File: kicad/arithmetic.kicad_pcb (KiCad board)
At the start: 2 copper layers, 49.5 x 53 mm, 71 parts, among them J1 Conn_01x03_Male, J2 Conn_01x05_Male, J3 Conn_01x05_Male, J4 Conn_Coaxial, J5 Conn_Coaxial, J6 Conn_Coaxial, U1 LM317, U2 LM337, U3 OPA197xD, U4 OPA197xD, U5 OPA197xD

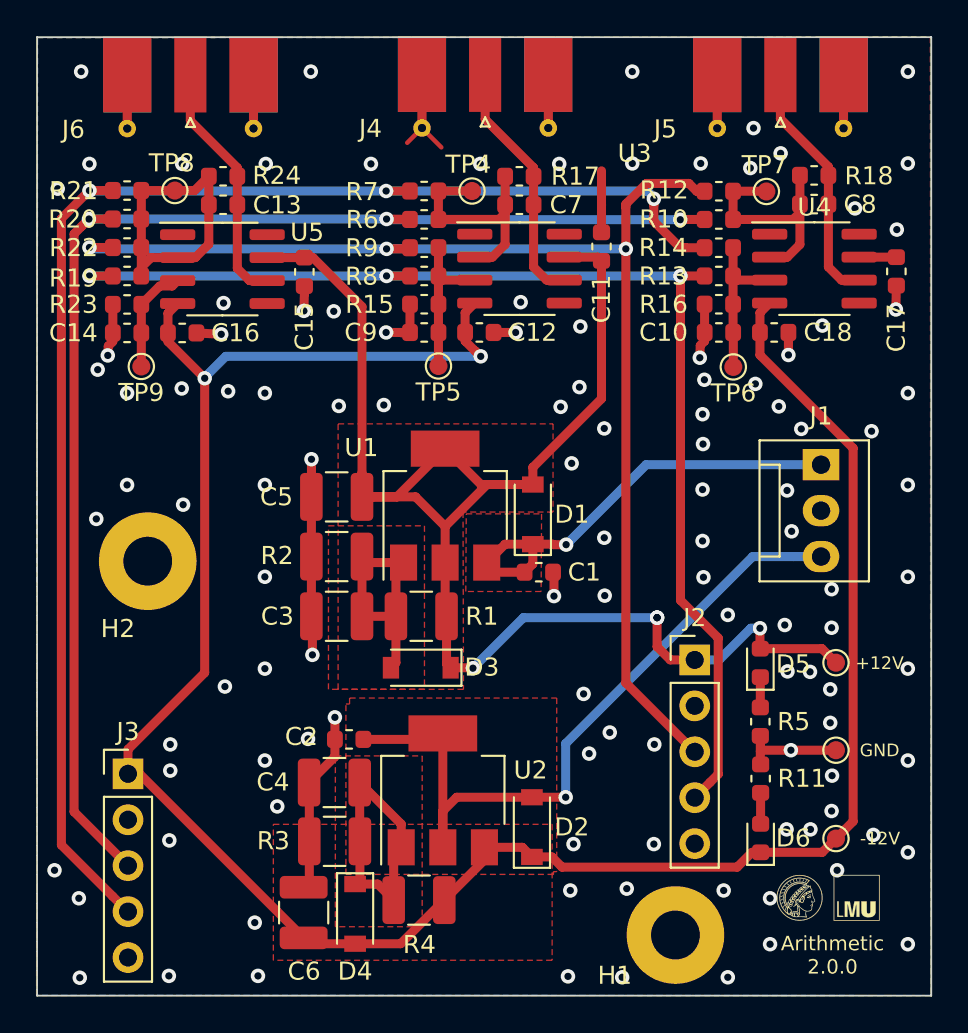
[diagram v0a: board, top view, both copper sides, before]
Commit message: moved detector mount on arithmetic to the right
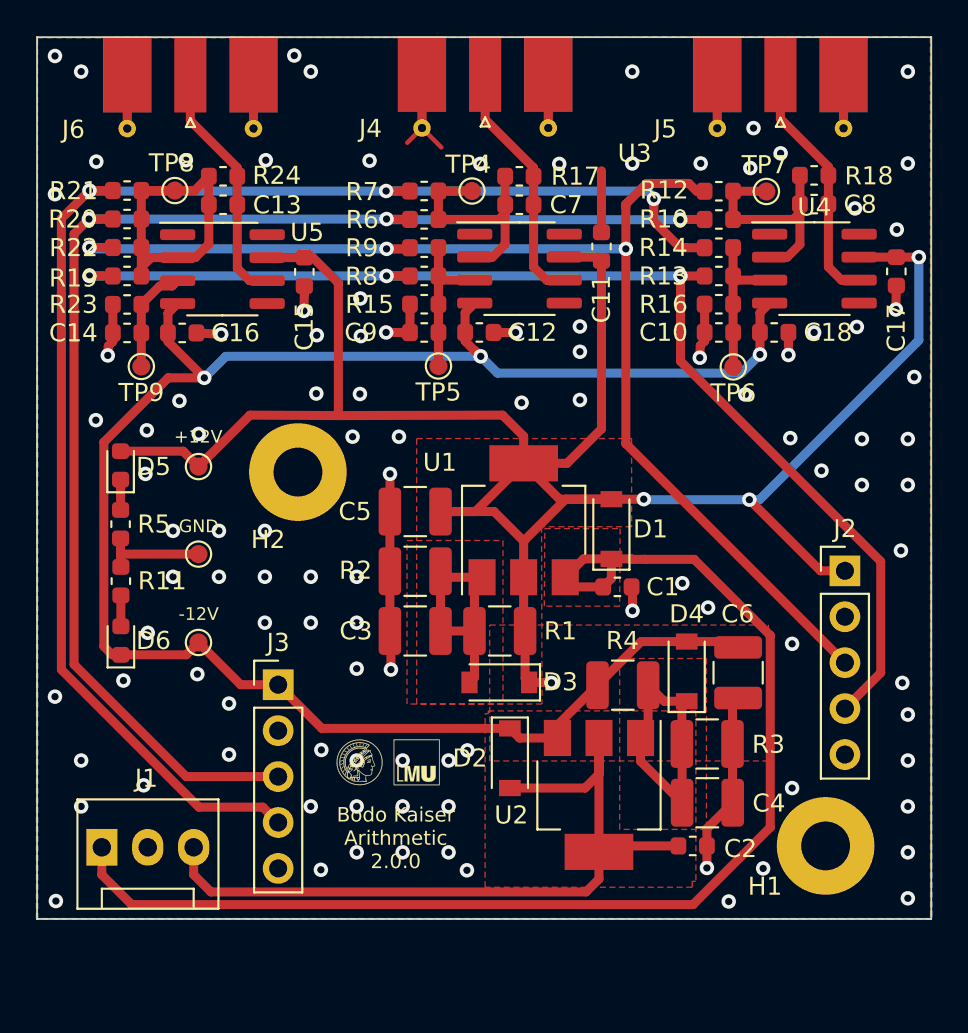
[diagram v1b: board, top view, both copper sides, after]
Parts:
- moved J1 45.1 mm to (77.3, 124.2), turned to 0 degrees
- moved R11 37.0 mm to (78.4, 109.5)
- moved D5 37.0 mm to (78.4, 103.1)
- moved D6 37.0 mm to (78.4, 112.7)
- moved R5 37.0 mm to (78.4, 106.3)
- moved +12V 36.9 mm to (82.7, 103.1)
- moved -12V 36.9 mm to (82.7, 112.9)
- moved GND 36.9 mm to (82.7, 108.0)
- moved C6 27.4 mm to (112.5, 114.5), turned to 90 degrees
- moved G*** 25.5 mm to (93.2, 119.5)
- moved D4 22.7 mm to (109.7, 114.5), turned to 90 degrees
- moved R3 21.3 mm to (110.8, 118.5), turned to 180 degrees
- moved C4 20.7 mm to (110.8, 121.7), turned to 180 degrees
- moved C2 19.9 mm to (110.0, 124.1), turned to 180 degrees
- moved R4 16.4 mm to (106.2, 115.2), turned to 180 degrees
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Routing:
- net +15V: track 24.8 -> 69.1 mm, vias 1 -> 0
- net +12V: track 92.0 -> 121.4 mm
- net -12V: track 127.4 -> 102.8 mm, vias 2 -> 3
- net -15V: track 41.3 -> 44.2 mm, vias 1 -> 0
- net /-X2: track 74.1 -> 75.6 mm
- net /-Y2: track 69.2 -> 67.7 mm
- net /-X1: track 66.9 -> 66.0 mm
- net /-Y1: track 80.9 -> 81.5 mm
- net GND: track 68.3 -> 68.4 mm, vias 116 -> 108
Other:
- board size 49.5 x 53 mm -> 49.5 x 48.8 mm
- board text added: "Bodo Kaiser Arithmetic 2.0.0"
- board text removed: "Arithmetic 2.0.0"

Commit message: fix some DRC errors, remove some test points
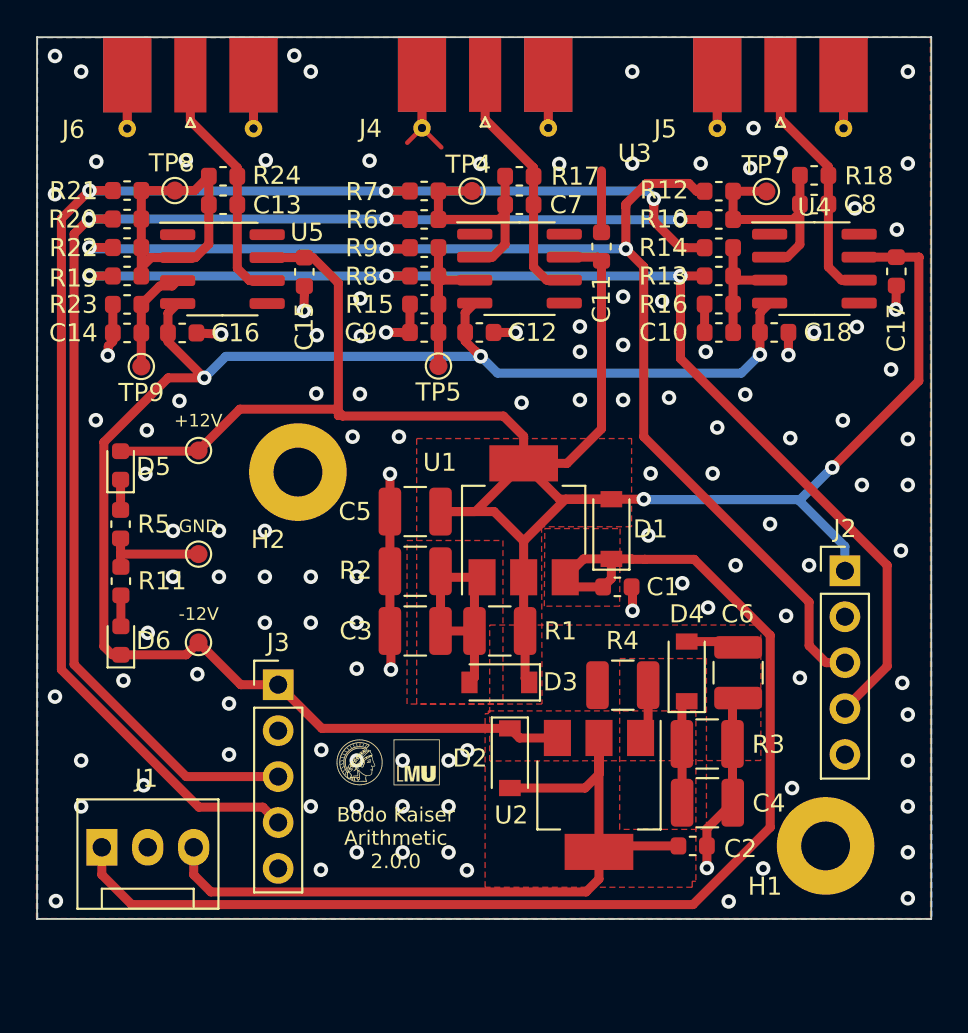
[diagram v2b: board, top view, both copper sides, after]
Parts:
- removed TP6: DIFFY+, TestPoint:TestPoint_Pad_D1.0mm
- moved +12V 0.89 mm to (82.7, 102.2)
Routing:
- net -12V: track 102.8 -> 93.0 mm
- net Net-(C4-Pad2): track 15.9 -> 8.82 mm
- net +12V: track 121.4 -> 119.2 mm, vias 4 -> 2
- net Net-(C10-Pad2): track 8.71 -> 6.80 mm
- net GND: track 68.4 -> 66.9 mm, vias 108 -> 119
- net /-Y2: track 67.7 -> 68.4 mm

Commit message: applied suggestions from Bodo Hecker
* changed R23 to 2k
* replaced pin holes in detector with padded pin holes
* increased casing of led resistors to 1210
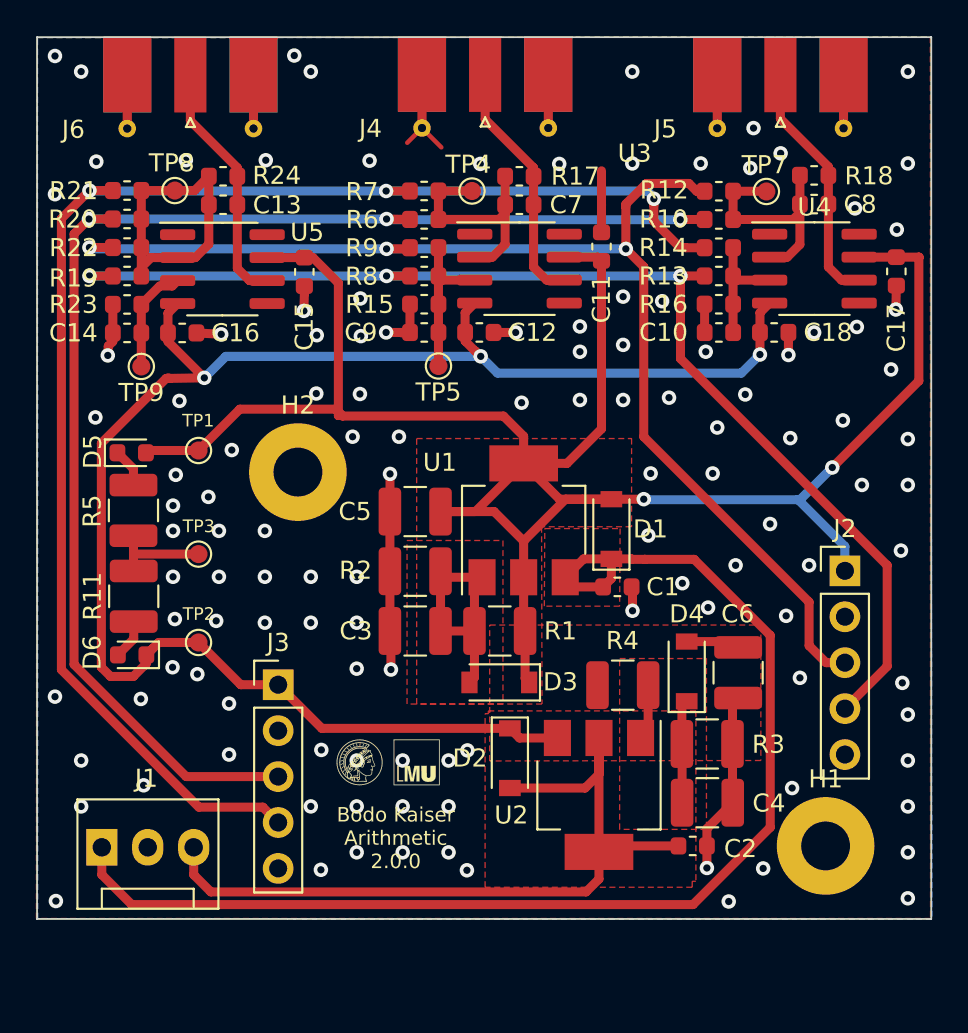
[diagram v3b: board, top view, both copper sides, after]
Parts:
- R11, R5: footprint Resistor_SMD:R_0603_1608Metric -> Resistor_SMD:R_1210_3225Metric
- R23: value 10k -> 2k
- moved R11 1.10 mm to (79.1, 110.3)
- moved R5 1.04 mm to (79.1, 105.5)
- moved D6 1.01 mm to (79.0, 113.5), turned to 180 degrees
- moved D5 0.93 mm to (79.0, 102.4), turned to 0 degrees
- renumbered +12V to TP1, -12V to TP2, GND to TP3
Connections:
- H1 pad 1: (no net) -> GND
- H2 pad 1: (no net) -> GND
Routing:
- net -12V: track 93.0 -> 95.8 mm
- net +12V: track 119.2 -> 118.2 mm
- net GND: track 66.9 -> 66.6 mm, vias 119 -> 123
